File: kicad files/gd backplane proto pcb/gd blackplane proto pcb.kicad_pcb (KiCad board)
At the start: 2 copper layers, 67.3 x 93 mm, 29 parts, among them J1 Pwr, J10 CTRL1, J12 Pwr, J13 CTRL2, J14 Addr_Main_Data, J15 CTRL1, J17 Pwr, J18 CTRL2, J19 Addr_Main_Data, J2 CTRL2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

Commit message: backplane rev1 complete
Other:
- board size 67.3 x 93 mm -> 64.9 x 93 mm
- board text added: "GD Debug Plane r1 2021-08-27 @baldengineer"
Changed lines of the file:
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@@
   (general
     (thickness 1.6)
-    (drawings 345)
+    (drawings 346)
     (tracks 707)
     (zones 0)
@@
     )
   )
-  (gr_arc (start 34.544 119.38) (end 33.02 119.38) (angle -90) (layer Edge.Cuts) (width 0.1))
-  (gr_arc (start 98.806 119.38) (end 98.806 120.904) (angle -90) (layer Edge.Cuts) (width 0.1))
-  (gr_arc (start 98.806 29.464) (end 100.33 29.464) (angle -90) (layer Edge.Cuts) (width 0.1))
-  (gr_arc (start 34.544 29.464) (end 34.544 27.94) (angle -90) (layer Edge.Cuts) (width 0.1))
+  (gr_text "GD Debug Plane r1\n2021-08-27\n@baldengineer" (at 69.215 59.0042) (layer F.SilkS)
+    (effects (font (size 0.8 0.8) (thickness 0.2)) (justify left))
+  )
+  (gr_arc (start 35.0266 119.38) (end 33.5026 119.38) (angle -90) (layer Edge.Cuts) (width 0.1))
+  (gr_arc (start 96.8502 119.38) (end 96.8502 120.904) (angle -90) (layer Edge.Cuts) (width 0.1))
+  (gr_arc (start 96.8502 29.464) (end 98.3742 29.464) (angle -90) (layer Edge.Cuts) (width 0.1))
+  (gr_arc (start 35.0266 29.464) (end 35.0266 27.94) (angle -90) (layer Edge.Cuts) (width 0.1))
   (gr_poly (pts (xy 102.362 117.856) (xy 30.226 117.856) (xy 30.226 120.396) (xy 102.362 120.396)) (layer B.SilkS) (width 0.1))
   (gr_poly (pts (xy 102.362 120.396) (xy 30.226 120.396) (xy 30.226 117.856) (xy 102.362 117.856)) (layer F.SilkS) (width 0.1))
@@
     (effects (font (size 0.8 0.8) (thickness 0.2)))
   )
-  (gr_line (start 33.02 119.38) (end 33.02 29.464) (layer Edge.Cuts) (width 0.1))
-  (gr_line (start 98.806 120.904) (end 34.544 120.904) (layer Edge.Cuts) (width 0.1))
-  (gr_line (start 100.33 29.464) (end 100.33 119.38) (layer Edge.Cuts) (width 0.1))
-  (gr_line (start 34.544 27.94) (end 98.806 27.94) (layer Edge.Cuts) (width 0.1))
+  (gr_line (start 33.5026 119.38) (end 33.5026 29.464) (layer Edge.Cuts) (width 0.1))
+  (gr_line (start 96.8502 120.904) (end 35.0266 120.904) (layer Edge.Cuts) (width 0.1))
+  (gr_line (start 98.3742 29.464) (end 98.3742 119.38) (layer Edge.Cuts) (width 0.1))
+  (gr_line (start 35.0266 27.94) (end 96.8502 27.94) (layer Edge.Cuts) (width 0.1))
   (via (at 59.69 39.878) (size 0.8) (drill 0.4) (layers F.Cu B.Cu) (net 1))
   (segment (start 59.37 39.558) (end 59.69 39.878) (width 0.2032) (layer F.Cu) (net 1))

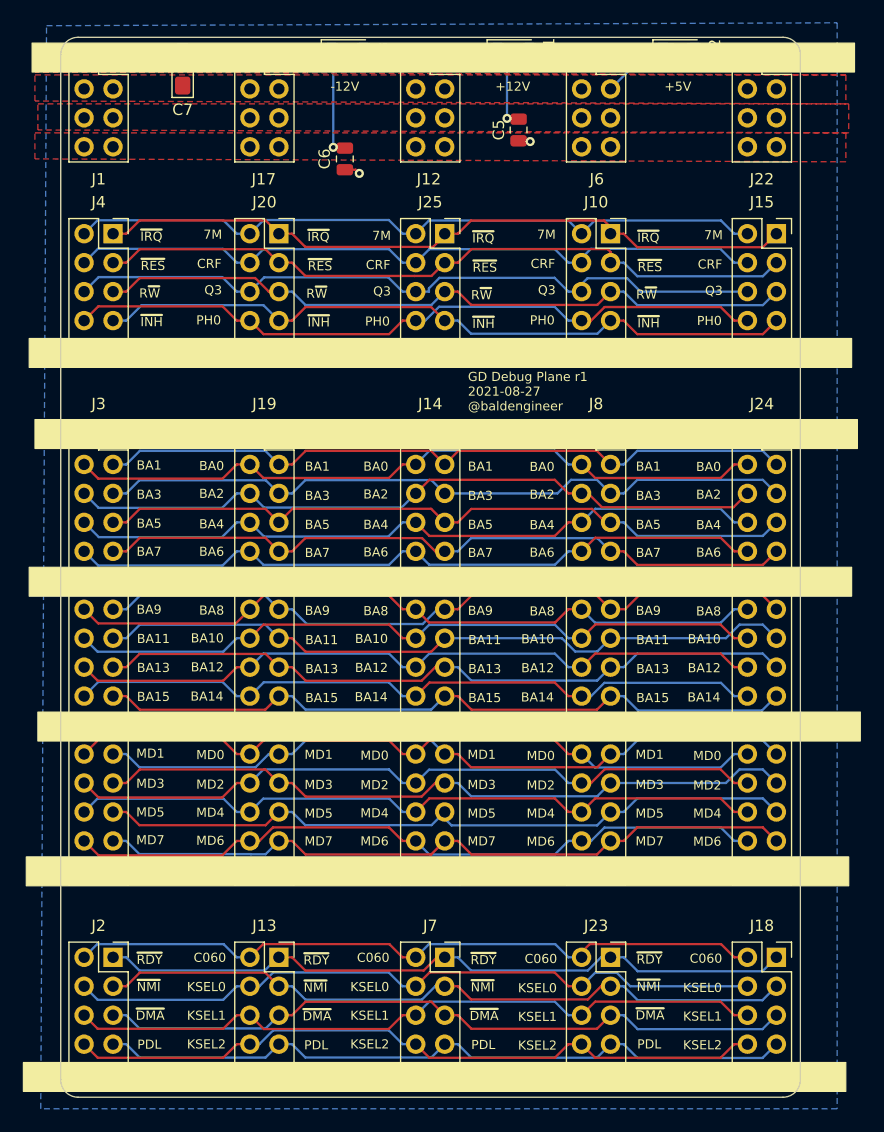
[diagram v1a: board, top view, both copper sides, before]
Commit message: flipped first connector on protoboard to match reversed pinout on the main board.
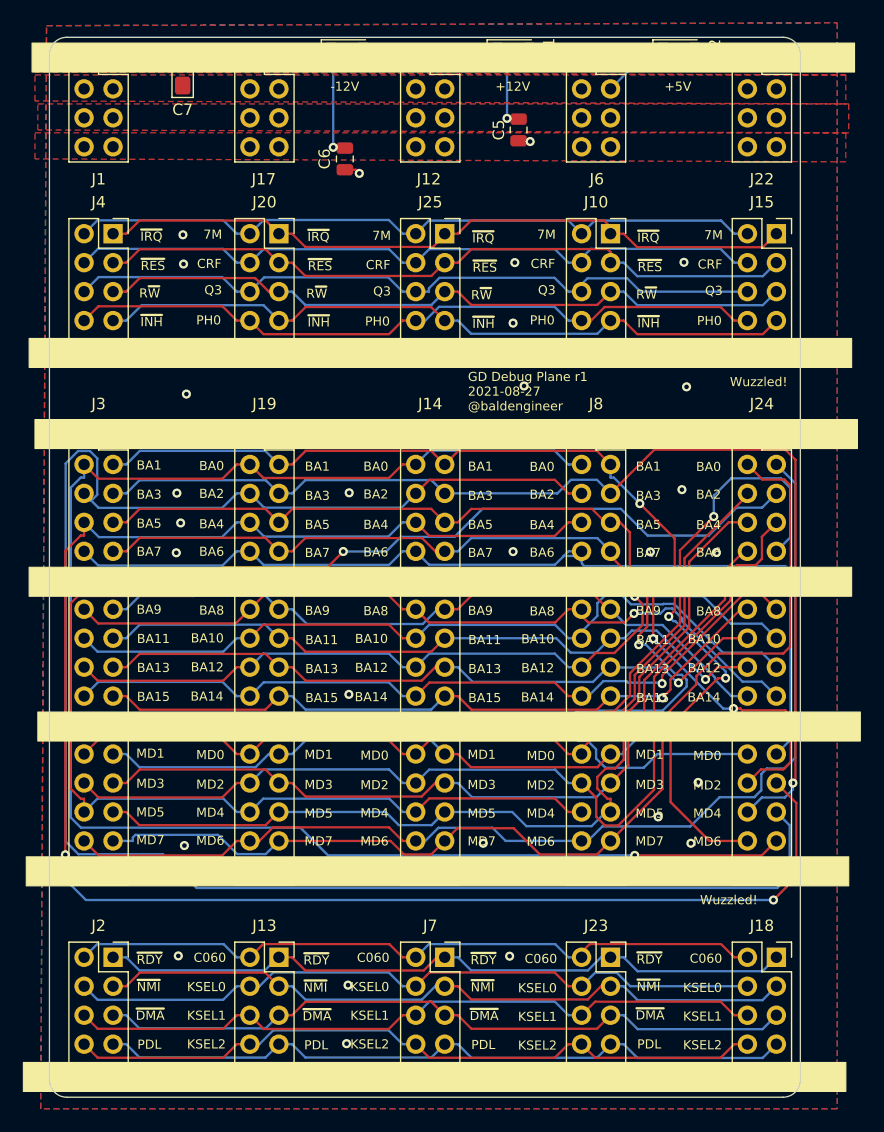
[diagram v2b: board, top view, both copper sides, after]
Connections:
- J24 pad 10: /BA6 -> /MD1
- J24 pad 13: /BA9 -> /BA14
- J24 pad 14: /BA8 -> /BA15
- J24 pad 15: /BA11 -> /BA12
- J24 pad 16: /BA10 -> /BA13
- J24 pad 17: /BA13 -> /BA10
- J24 pad 18: /BA12 -> /BA11
- J24 pad 19: /BA15 -> /BA8
- J24 pad 20: /BA14 -> /BA9
- J24 pad 23: /MD1 -> /BA6
- J24 pad 24: /MD0 -> /BA7
- J24 pad 25: /MD3 -> /BA4
- J24 pad 26: /MD2 -> /BA5
- J24 pad 27: /MD5 -> /BA2
- J24 pad 28: /MD4 -> /BA3
- J24 pad 29: /MD7 -> /BA0
- J24 pad 3: /BA1 -> /MD6
- J24 pad 30: /MD6 -> /BA1
- J24 pad 4: /BA0 -> /MD7
- J24 pad 5: /BA3 -> /MD4
- J24 pad 6: /BA2 -> /MD5
- J24 pad 7: /BA5 -> /MD2
- J24 pad 8: /BA4 -> /MD3
- J24 pad 9: /BA7 -> /MD0
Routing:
- net GND: track 3.50 -> 200.9 mm, vias 3 -> 34
- net /BA2: track 62.3 -> 159.0 mm
- net /BA4: track 62.3 -> 153.6 mm, vias 0 -> 2
- net /BA0: track 62.2 -> 142.1 mm, vias 0 -> 1
- net /MD4: track 62.1 -> 133.4 mm, vias 0 -> 1
- net /BA3: track 62.1 -> 98.5 mm, vias 0 -> 1
- net /MD6: track 62.2 -> 95.6 mm
- net /MD7: track 62.1 -> 93.7 mm
- net /BA7: track 62.1 -> 93.6 mm, vias 0 -> 1
- net /BA1: track 62.1 -> 91.6 mm, vias 0 -> 3
- net /MD0: track 62.2 -> 88.5 mm, vias 0 -> 1
- net /MD2: track 62.2 -> 85.7 mm
- net /BA6: track 62.2 -> 83.7 mm
- net /BA5: track 62.1 -> 82.3 mm, vias 0 -> 2
- net /MD5: track 62.4 -> 81.1 mm
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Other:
- board size 64.9 x 93 mm -> 65.9 x 93 mm
- board text added: "Wuzzled!"

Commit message: Rev2 added port, made bigger, re-did wuzzle field
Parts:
- added J11: CTRL1, Connector_PinSocket_2.54mm:PinSocket_2x05_P2.54mm_Vertical, F.Cu at (141.7, 42.6)
- added J16: Addr_Main_Data, Connector_PinSocket_2.54mm:PinSocket_2x16_P2.54mm_Vertical, F.Cu at (141.7, 60.3)
- added J5: Pwr, Connector_PinSocket_2.54mm:PinSocket_2x04_P2.54mm_Vertical, F.Cu at (141.7, 27.4)
- added J9: CTRL2, Connector_PinSocket_2.54mm:PinSocket_2x05_P2.54mm_Vertical, F.Cu at (141.7, 106.1)
- moved C7 207.2 mm to (251.3, 28.5)
- moved J22 165.1 mm to (261.4, 27.4)
- moved J15 165.1 mm to (261.4, 42.6)
- moved J18 165.1 mm to (261.4, 106.1)
- moved J24 165.1 mm to (261.4, 60.3)
- moved R2 157.1 mm to (244.9, 26.7)
- moved R3 156.6 mm to (215.2, 26.8)
- moved D2 156.6 mm to (244.3, 26.8)
- moved C6 156.5 mm to (214.9, 36.0)
- moved D3 156.0 mm to (214.6, 26.8)
- moved J10 149.1 mm to (230.8, 42.6)
- moved J23 149.1 mm to (230.8, 106.1)
- moved J6 149.1 mm to (230.8, 27.4)
- moved J8 149.1 mm to (230.8, 60.3)
- moved J12 133.9 mm to (201.1, 27.4)
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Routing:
- net GND: track 200.9 -> 2.91 mm, vias 34 -> 21
- net /BA1: track 91.6 -> 192.9 mm, vias 3 -> 0
- net /BA8: track 68.6 -> 167.9 mm, vias 1 -> 0
- net /BA5: track 82.3 -> 179.9 mm, vias 2 -> 0
- net /BA9: track 62.0 -> 158.6 mm
- net /BA15: track 62.4 -> 156.1 mm
- net /BA10: track 69.1 -> 162.6 mm
- net /C060-67: track 62.3 -> 155.6 mm
- net /~NMI: track 62.1 -> 155.3 mm
- net /~DMA: track 62.1 -> 155.3 mm
- net /PDLTRIG: track 62.1 -> 155.2 mm
- net /~RDY: track 62.1 -> 154.9 mm
- net /KSEL1: track 62.1 -> 154.9 mm
- net /KSEL0: track 62.2 -> 154.9 mm
- net /MD0: track 88.5 -> 181.1 mm, vias 1 -> 0
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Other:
- board size 65.9 x 93 mm -> 155.4 x 93 mm
- board text added: "GD Debug Plane rev2 2022-02-08 @baldengineer"
- board text removed: "GD Debug Plane r1 2021-08-27 @baldengineer"
